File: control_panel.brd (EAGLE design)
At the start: 62.1 x 66 mm, 44 parts, among them J1 AVR_SPI_PRG_6NS, Q1 L78M05CDT, U1 LTC4412ES6TRMPBF, U2 NX2301P, U3 NX2301P

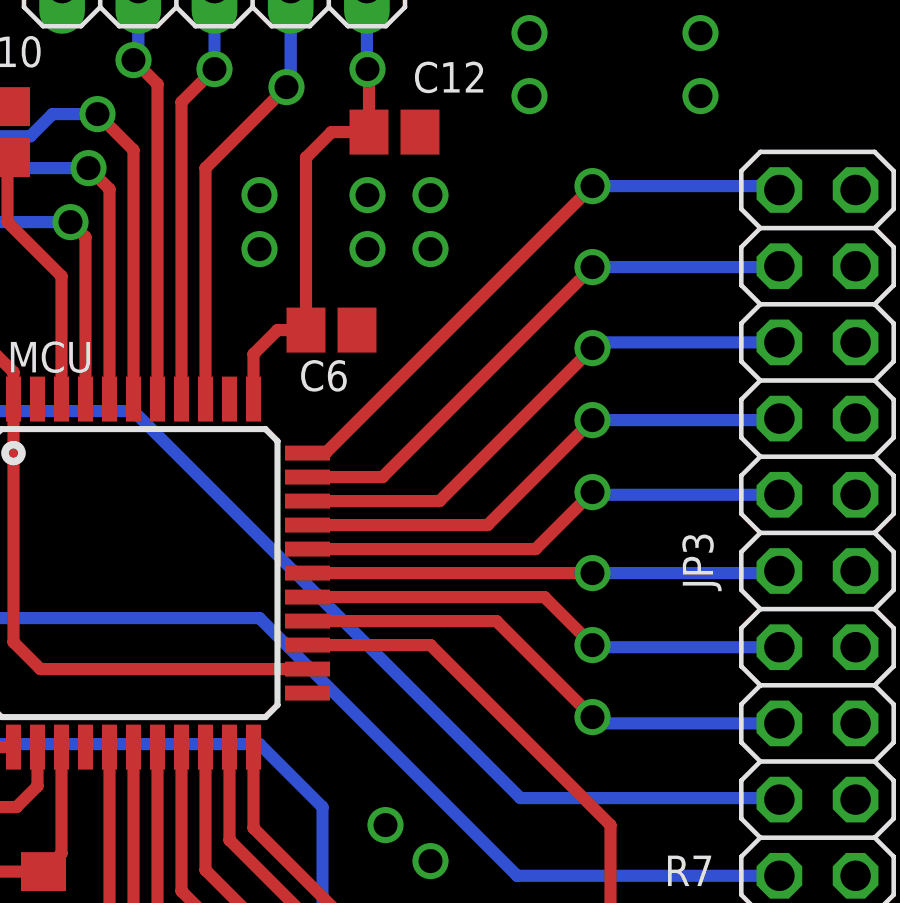
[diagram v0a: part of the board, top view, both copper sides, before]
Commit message: Widened supply wires on the driver, changed wire positions on control panel board.
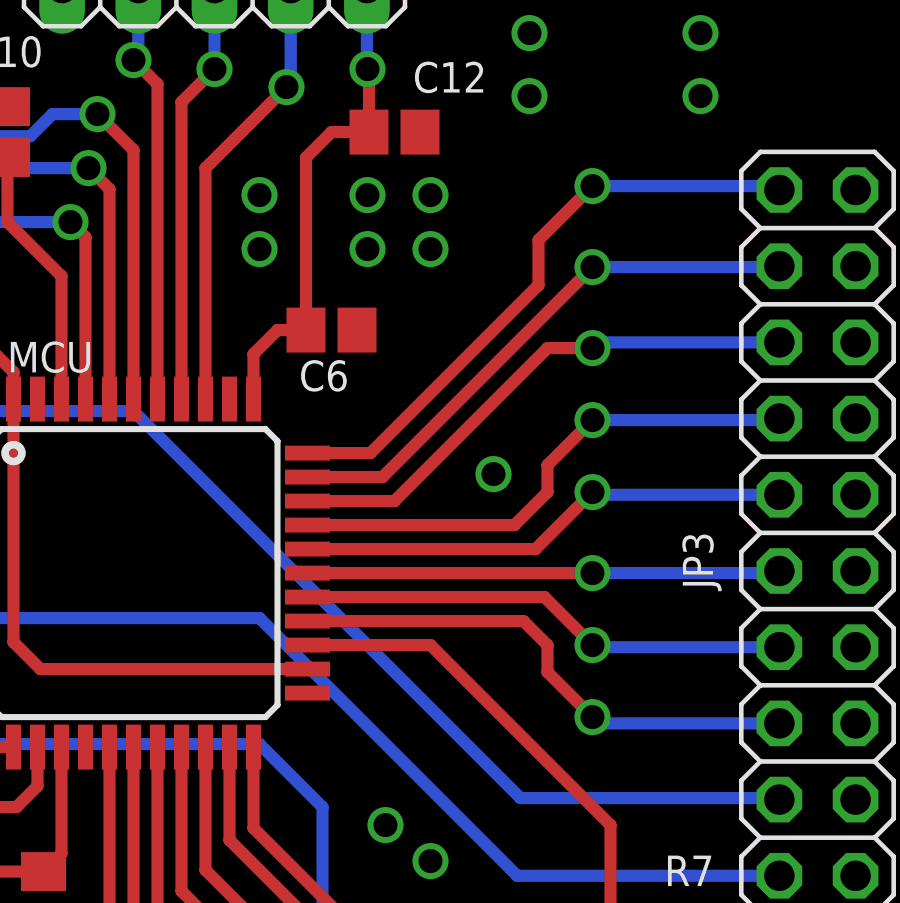
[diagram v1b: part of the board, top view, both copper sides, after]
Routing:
- net BTN_6: track 19.5 -> 20.3 mm
- net BTN_CAM_LEFT: track 17.1 -> 17.7 mm
- net BTN_CAM_CENTER: track 17.2 -> 17.7 mm
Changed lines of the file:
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@@
 <via x="22.2" y="8.7" extent="1-16" drill="0.8"/>
 <contactref element="X1" pad="2"/>
+<via x="44.7" y="44.4" extent="1-16" drill="0.8"/>
 </signal>
 <signal name="V_EXT">
@@
 <contactref element="MCU" pad="26"/>
 <contactref element="JP3" pad="10"/>
-<wire x1="38.5" y1="39.5" x2="44.8" y2="39.5" width="0.4064" layer="1"/>
-<wire x1="44.8" y1="39.5" x2="48" y2="36.3" width="0.4064" layer="1"/>
+<wire x1="38.5" y1="39.5" x2="45.7" y2="39.5" width="0.4064" layer="1"/>
 <via x="48" y="36.3" extent="1-16" drill="0.8" shape="square"/>
 <wire x1="54.23" y1="36.09" x2="48.21" y2="36.09" width="0.4064" layer="16"/>
 <wire x1="48.21" y1="36.09" x2="48" y2="36.3" width="0.4064" layer="16"/>
+<wire x1="45.7" y1="39.5" x2="46.5" y2="38.7" width="0.4064" layer="1"/>
+<wire x1="46.5" y1="38.7" x2="46.5" y2="37.8" width="0.4064" layer="1"/>
+<wire x1="46.5" y1="37.8" x2="48" y2="36.3" width="0.4064" layer="1"/>
 </signal>
 <signal name="BTN_CAM_RIGHT">
@@
 <contactref element="MCU" pad="30"/>
 <contactref element="JP3" pad="18"/>
-<wire x1="38.5" y1="42.7" x2="44.5" y2="42.7" width="0.4064" layer="1"/>
-<wire x1="44.5" y1="42.7" x2="48" y2="46.2" width="0.4064" layer="1"/>
+<wire x1="38.5" y1="42.7" x2="45.4" y2="42.7" width="0.4064" layer="1"/>
 <via x="48" y="46.2" extent="1-16" drill="0.8" shape="square"/>
 <wire x1="48" y1="46.2" x2="54.18" y2="46.2" width="0.4064" layer="16"/>
 <wire x1="54.18" y1="46.2" x2="54.23" y2="46.25" width="0.4064" layer="16"/>
+<wire x1="45.4" y1="42.7" x2="46.5" y2="43.8" width="0.4064" layer="1"/>
+<wire x1="46.5" y1="43.8" x2="46.5" y2="44.7" width="0.4064" layer="1"/>
+<wire x1="46.5" y1="44.7" x2="48" y2="46.2" width="0.4064" layer="1"/>
 </signal>
 <signal name="DO+">
@@
 <contactref element="MCU" pad="31"/>
 <contactref element="JP3" pad="20"/>
-<wire x1="38.5" y1="43.5" x2="42.9" y2="43.5" width="0.4064" layer="1"/>
-<wire x1="42.9" y1="43.5" x2="48" y2="48.6" width="0.4064" layer="1"/>
 <via x="48" y="48.6" extent="1-16" drill="0.8" shape="square"/>
 <wire x1="54.23" y1="48.79" x2="48.19" y2="48.79" width="0.4064" layer="16"/>
 <wire x1="48.19" y1="48.79" x2="48" y2="48.6" width="0.4064" layer="16"/>
+<wire x1="38.5" y1="43.5" x2="41.4" y2="43.5" width="0.4064" layer="1"/>
+<wire x1="41.4" y1="43.5" x2="46.5" y2="48.6" width="0.4064" layer="1"/>
+<wire x1="46.5" y1="48.6" x2="48" y2="48.6" width="0.4064" layer="1"/>
 </signal>
 <signal name="SCL">
@@
 <wire x1="48" y1="54" x2="54.1" y2="54" width="0.4064" layer="16"/>
 <wire x1="54.1" y1="54" x2="54.23" y2="53.87" width="0.4064" layer="16"/>
-<wire x1="38.5" y1="45.1" x2="39.1" y2="45.1" width="0.4064" layer="1"/>
-<wire x1="39.1" y1="45.1" x2="48" y2="54" width="0.4064" layer="1"/>
+<wire x1="38.5" y1="45.1" x2="40.6" y2="45.1" width="0.4064" layer="1"/>
+<wire x1="40.6" y1="45.1" x2="46.2" y2="50.7" width="0.4064" layer="1"/>
+<wire x1="46.2" y1="50.7" x2="46.2" y2="52.2" width="0.4064" layer="1"/>
+<wire x1="46.2" y1="52.2" x2="48" y2="54" width="0.4064" layer="1"/>
 </signal>
 <signal name="N$9">
